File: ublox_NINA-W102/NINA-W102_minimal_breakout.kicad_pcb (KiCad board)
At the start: 2 copper layers, 47 x 20.7 mm, 17 parts, among them J1 Conn_01x15, J2 Conn_01x15, J3 6_PIN_SERIAL_TARGETLOCK, SW1 BOOT, SW2 RESET, U1 NINA-W102

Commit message: Added revision info on front PCB
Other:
- board text added: "rev.0.3"
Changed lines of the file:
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@@
     (area 104.064999 95.987799 151.205001 116.864201)
     (thickness 1.6)
-    (drawings 41)
+    (drawings 42)
     (tracks 480)
     (zones 0)
@@
       (xy 0.88646 0.23114)) (layer F.SilkS) (width 0.01))
   )
+  (gr_text rev.0.3 (at 123.2916 106.7816 90) (layer F.SilkS)
+    (effects (font (size 0.8 0.8) (thickness 0.127)))
+  )
   (gr_line (start 151.13 112.3442) (end 146.8882 116.7892) (layer Edge.Cuts) (width 0.15))

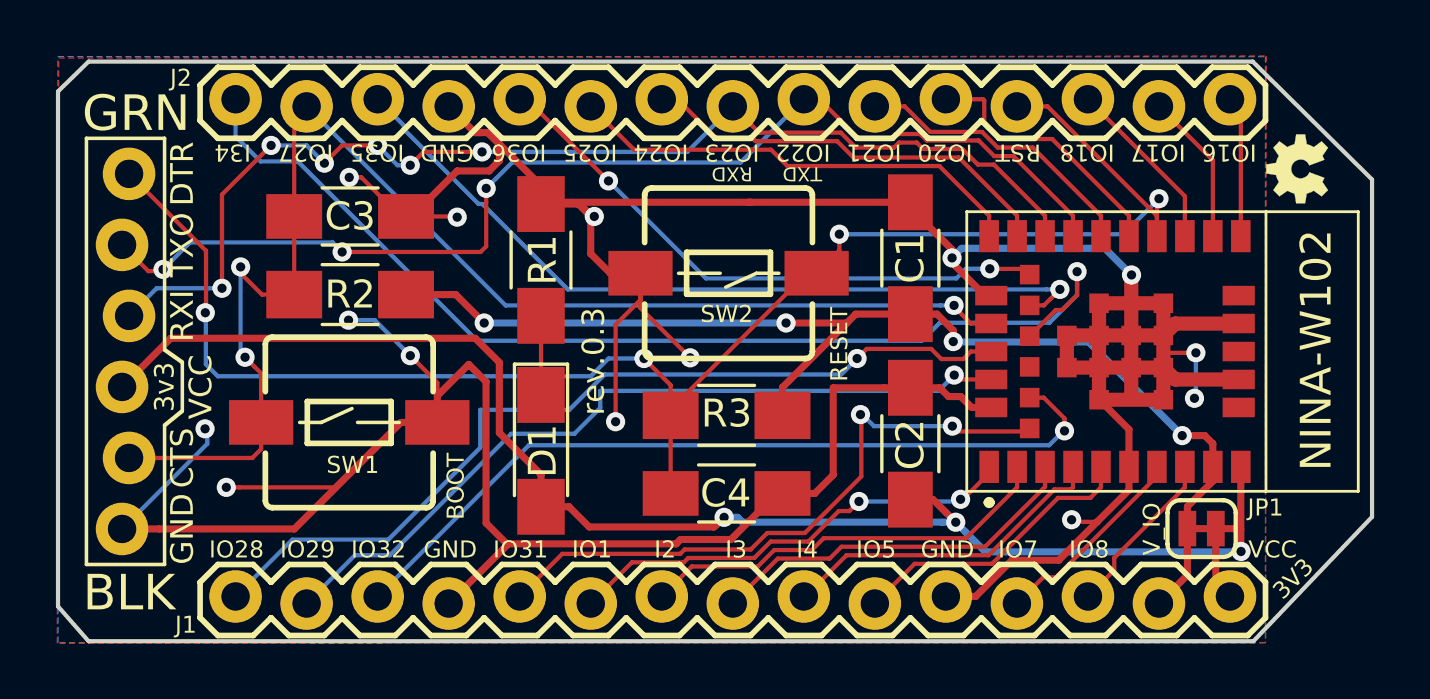
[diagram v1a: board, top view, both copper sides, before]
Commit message: Added some silk labels for pins from datasheet
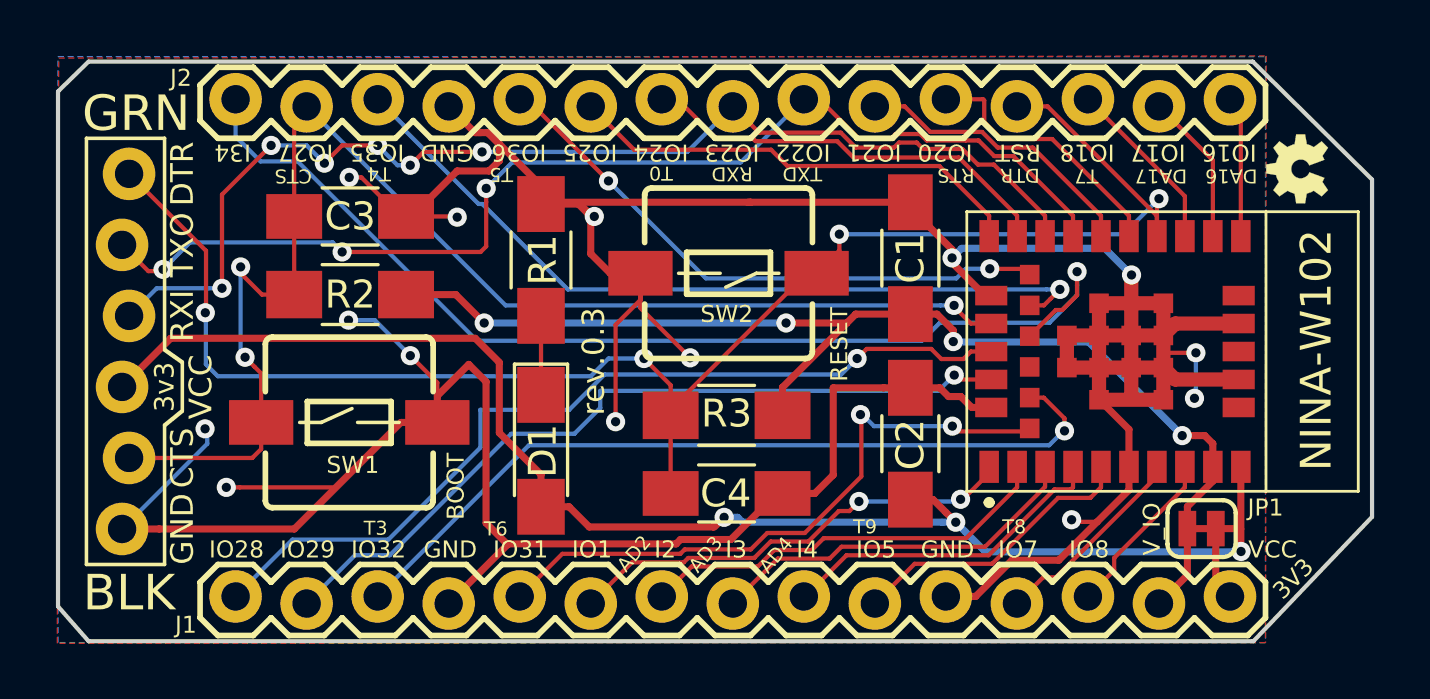
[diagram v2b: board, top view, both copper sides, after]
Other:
- board text added: "AD2"
- board text added: "AD3"
- board text added: "AD4"
- board text added: "CTS"
- board text added: "DA16"
- board text added: "DA17"
- board text added: "DTR"
- board text added: "RTS"
- board text added: "T0"
- board text added: "T3"
- board text added: "T4"
- board text added: "T5"
- board text added: "T6"
- board text added: "T7"
- board text added: "T8"
- board text added: "T9"
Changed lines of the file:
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@@
     (area 104.064999 95.987799 151.205001 116.864201)
     (thickness 1.6)
-    (drawings 42)
+    (drawings 58)
     (tracks 480)
     (zones 0)
@@
       (xy 0.88646 0.23114)) (layer F.SilkS) (width 0.01))
   )
+  (gr_text T5 (at 119.5578 100.1014 180) (layer F.SilkS)
+    (effects (font (size 0.5 0.5) (thickness 0.12)) (justify right))
+  )
+  (gr_text T4 (at 115.189 100.076 180) (layer F.SilkS)
+    (effects (font (size 0.5 0.5) (thickness 0.12)) (justify right))
+  )
+  (gr_text T3 (at 115.9256 112.7506) (layer F.SilkS)
+    (effects (font (size 0.5 0.5) (thickness 0.12)) (justify right))
+  )
+  (gr_text T6 (at 120.2182 112.776) (layer F.SilkS)
+    (effects (font (size 0.5 0.5) (thickness 0.12)) (justify right))
+  )
+  (gr_text T0 (at 125.2728 100.0506 180) (layer F.SilkS)
+    (effects (font (size 0.5 0.5) (thickness 0.12)) (justify right))
+  )
+  (gr_text RTS (at 135.5852 100.1268 180) (layer F.SilkS)
+    (effects (font (size 0.5 0.5) (thickness 0.12)) (justify right))
+  )
+  (gr_text T7 (at 140.4874 100.1522 180) (layer F.SilkS)
+    (effects (font (size 0.5 0.5) (thickness 0.12)) (justify right))
+  )
+  (gr_text DA17 (at 142.6464 100.1522 180) (layer F.SilkS)
+    (effects (font (size 0.5 0.5) (thickness 0.12)) (justify right))
+  )
+  (gr_text DA16 (at 145.161 100.1522 180) (layer F.SilkS)
+    (effects (font (size 0.5 0.5) (thickness 0.12)) (justify right))
+  )
+  (gr_text AD4 (at 130.2766 113.157 50) (layer F.SilkS)
+    (effects (font (size 0.5 0.5) (thickness 0.12)) (justify right))
+  )
+  (gr_text AD3 (at 127.762 113.1316 50) (layer F.SilkS)
+    (effects (font (size 0.5 0.5) (thickness 0.12)) (justify right))
+  )
+  (gr_text AD2 (at 125.1966 113.1062 50) (layer F.SilkS)
+    (effects (font (size 0.5 0.5) (thickness 0.12)) (justify right))
+  )
+  (gr_text T9 (at 133.4262 112.6998) (layer F.SilkS)
+    (effects (font (size 0.5 0.5) (thickness 0.12)) (justify right))
+  )
+  (gr_text T8 (at 138.7602 112.6998) (layer F.SilkS)
+    (effects (font (size 0.5 0.5) (thickness 0.12)) (justify right))
+  )
+  (gr_text CTS (at 111.887 100.1522 180) (layer F.SilkS)
+    (effects (font (size 0.5 0.5) (thickness 0.12)) (justify right))
+  )
+  (gr_text DTR (at 137.8204 100.1268 180) (layer F.SilkS)
+    (effects (font (size 0.5 0.5) (thickness 0.12)) (justify right))
+  )
   (gr_text rev.0.3 (at 123.2916 106.7816 90) (layer F.SilkS)

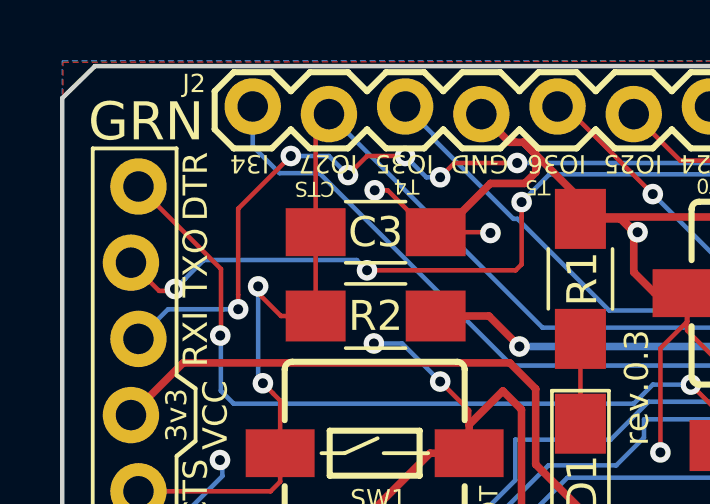
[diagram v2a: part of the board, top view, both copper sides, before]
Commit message: Added missing AD pin label
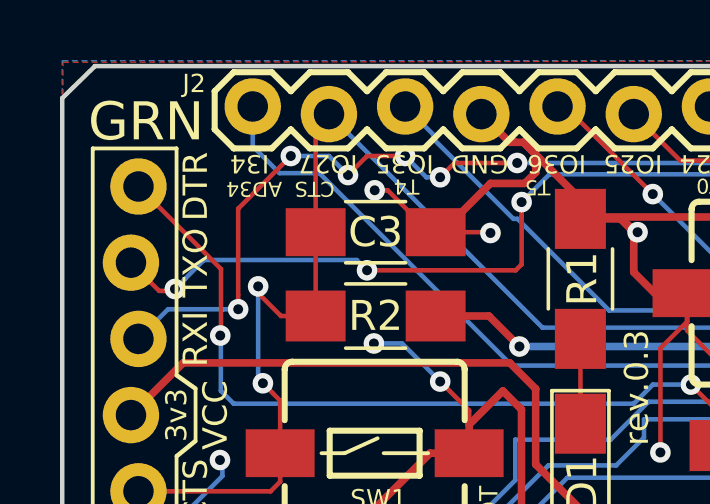
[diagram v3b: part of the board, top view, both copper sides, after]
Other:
- board text added: "AD34"
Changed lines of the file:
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@@
     (area 104.064999 95.987799 151.205001 116.864201)
     (thickness 1.6)
-    (drawings 58)
+    (drawings 59)
     (tracks 480)
     (zones 0)
@@
       (xy 0.88646 0.23114)) (layer F.SilkS) (width 0.01))
   )
+  (gr_text AD34 (at 109.601 100.1522 180) (layer F.SilkS)
+    (effects (font (size 0.5 0.5) (thickness 0.12)) (justify right))
+  )
   (gr_text T5 (at 119.5578 100.1014 180) (layer F.SilkS)

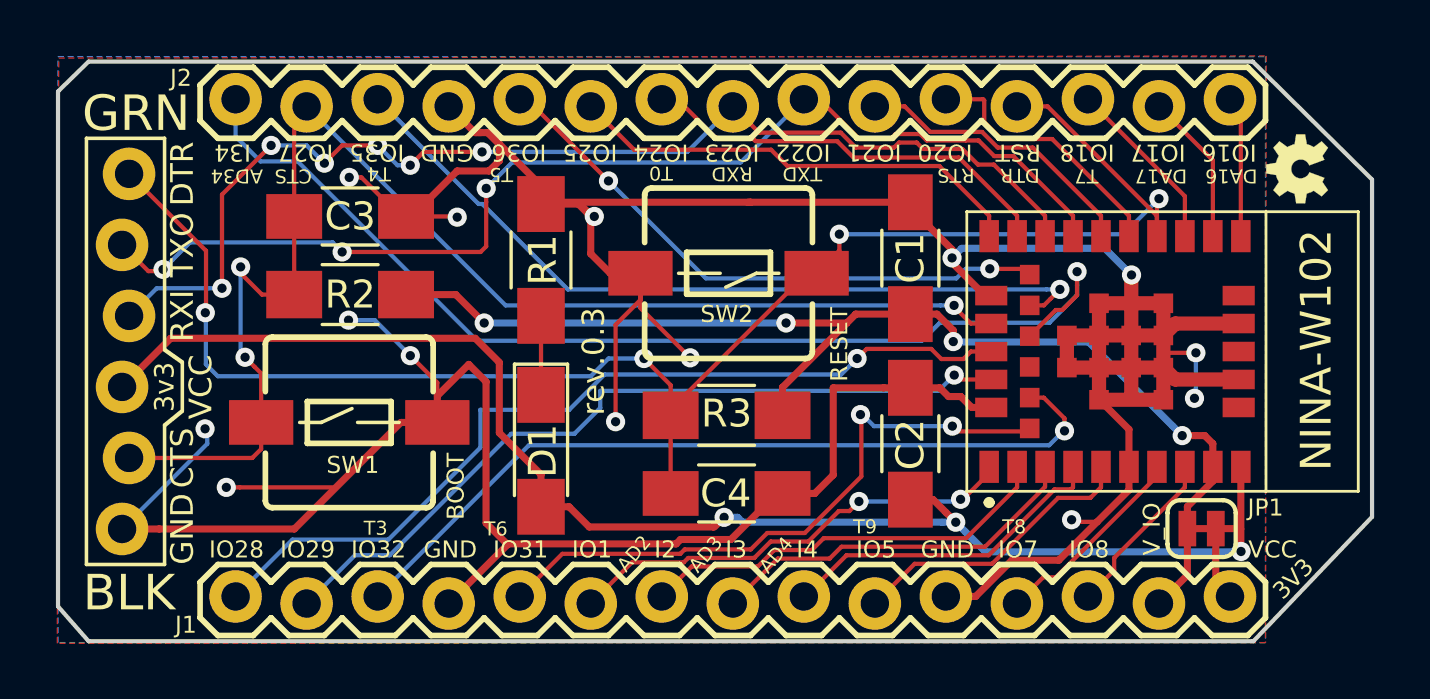
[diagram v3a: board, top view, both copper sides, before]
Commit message: Added dimensions and updated revision
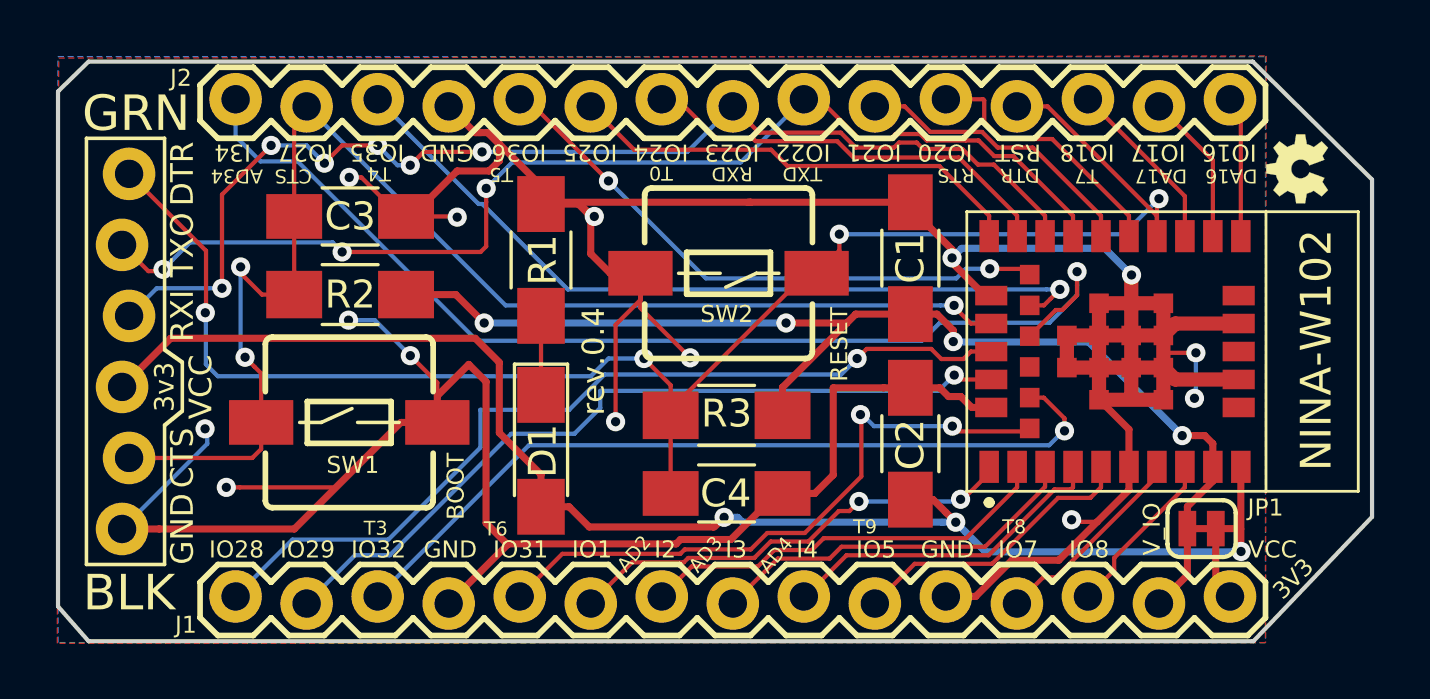
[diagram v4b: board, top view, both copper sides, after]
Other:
- board text added: "rev.0.4"
- board text removed: "rev.0.3"
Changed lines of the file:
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@@
     (area 104.064999 95.987799 151.205001 116.864201)
     (thickness 1.6)
-    (drawings 59)
+    (drawings 61)
     (tracks 480)
     (zones 0)
@@
   (title_block
     (title "ublox NINA-W102 minimal breakout")
-    (date 2018-04-21)
-    (rev 0.3)
+    (date 2018-04-22)
+    (rev 0.4)
     (company "GDG Zürich")
     (comment 1 "Michel Racic")
@@
       (xy 0.88646 0.23114)) (layer F.SilkS) (width 0.01))
   )
+  (dimension 46.8884 (width 0.3) (layer Dwgs.User)
+    (gr_text "46.888 mm" (at 127.6858 88.3628) (layer Dwgs.User)
+      (effects (font (size 1.5 1.5) (thickness 0.3)))
+    )
+    (feature1 (pts (xy 104.2416 100.33) (xy 104.2416 87.0128)))
+    (feature2 (pts (xy 151.13 100.33) (xy 151.13 87.0128)))
+    (crossbar (pts (xy 151.13 89.7128) (xy 104.2416 89.7128)))
+    (arrow1a (pts (xy 104.2416 89.7128) (xy 105.368104 89.126379)))
+    (arrow1b (pts (xy 104.2416 89.7128) (xy 105.368104 90.299221)))
+    (arrow2a (pts (xy 151.13 89.7128) (xy 150.003496 89.126379)))
+    (arrow2b (pts (xy 151.13 89.7128) (xy 150.003496 90.299221)))
+  )
+  (dimension 20.6502 (width 0.3) (layer Dwgs.User)
+    (gr_text "20.650 mm" (at 99.107 106.3879 270) (layer Dwgs.User)
+      (effects (font (size 1.5 1.5) (thickness 0.3)))
+    )
+    (feature1 (pts (xy 105.2576 116.713) (xy 97.757 116.713)))
+    (feature2 (pts (xy 105.2576 96.0628) (xy 97.757 96.0628)))
+    (crossbar (pts (xy 100.457 96.0628) (xy 100.457 116.713)))
+    (arrow1a (pts (xy 100.457 116.713) (xy 99.870579 115.586496)))
+    (arrow1b (pts (xy 100.457 116.713) (xy 101.043421 115.586496)))
+    (arrow2a (pts (xy 100.457 96.0628) (xy 99.870579 97.189304)))
+    (arrow2b (pts (xy 100.457 96.0628) (xy 101.043421 97.189304)))
+  )
   (gr_text AD34 (at 109.601 100.1522 180) (layer F.SilkS)
     (effects (font (size 0.5 0.5) (thickness 0.12)) (justify right))
@@
     (effects (font (size 0.5 0.5) (thickness 0.12)) (justify right))
   )
-  (gr_text rev.0.3 (at 123.2916 106.7816 90) (layer F.SilkS)
+  (gr_text rev.0.4 (at 123.2916 106.7816 90) (layer F.SilkS)
     (effects (font (size 0.8 0.8) (thickness 0.127)))
   )

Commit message: Simplified some tracks to look nicer
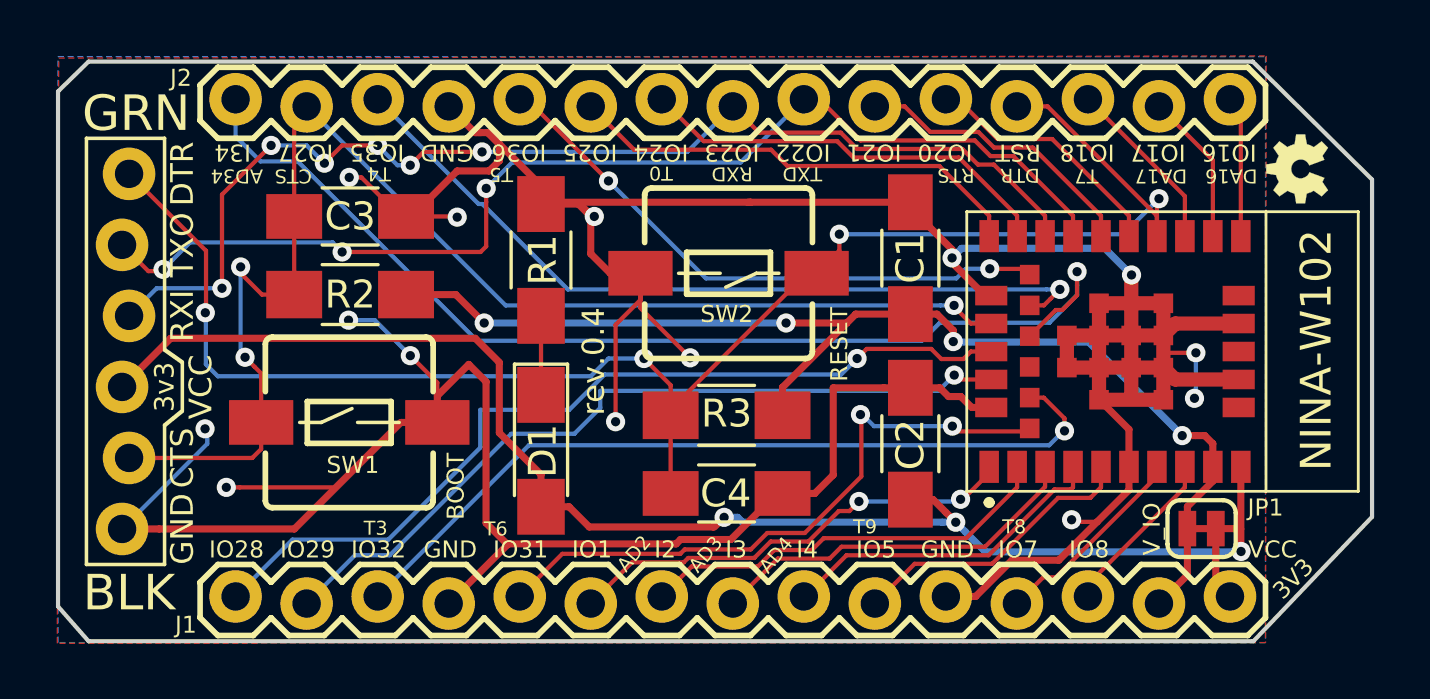
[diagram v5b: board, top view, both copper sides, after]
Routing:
- net Net-(J2-Pad11): track 9.45 -> 8.62 mm
